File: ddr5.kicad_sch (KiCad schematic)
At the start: 39 parts, among them U1 MT60B2G8HB-48B_A

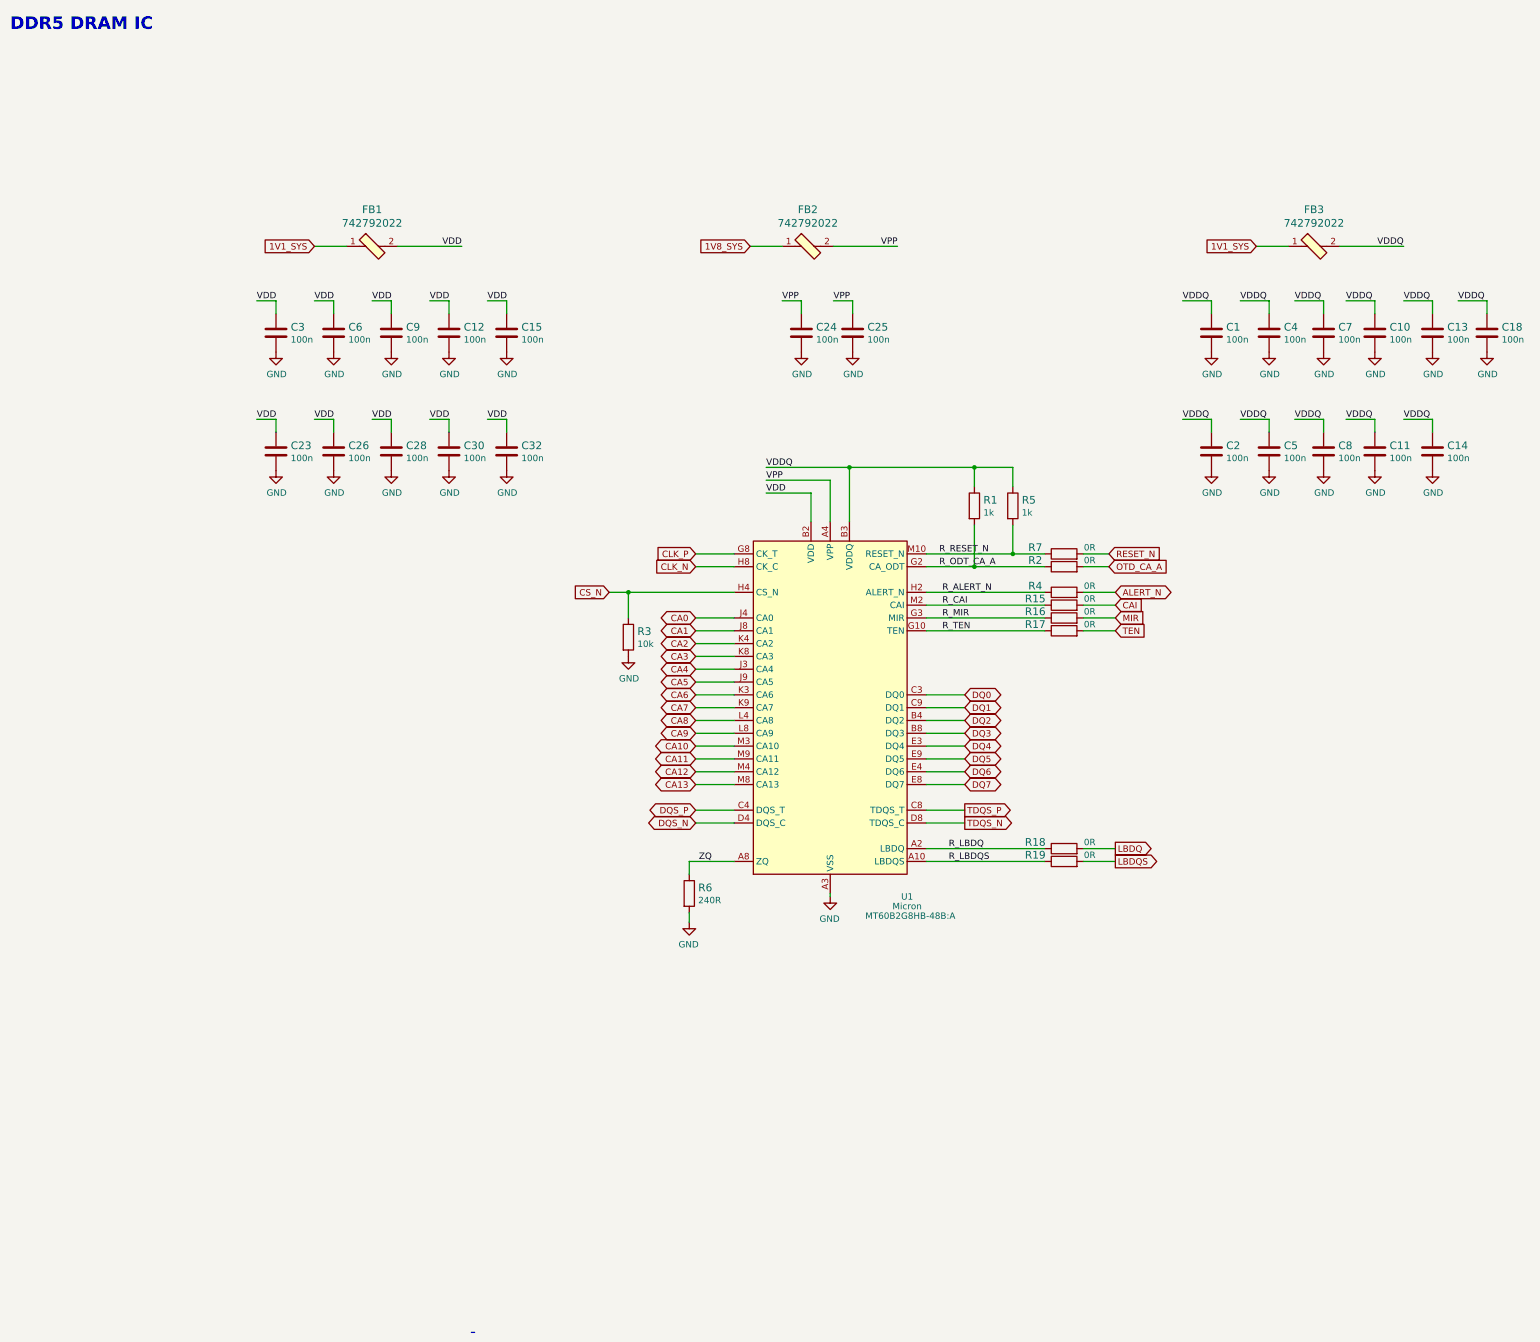
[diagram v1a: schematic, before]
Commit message: Introduce component standardization
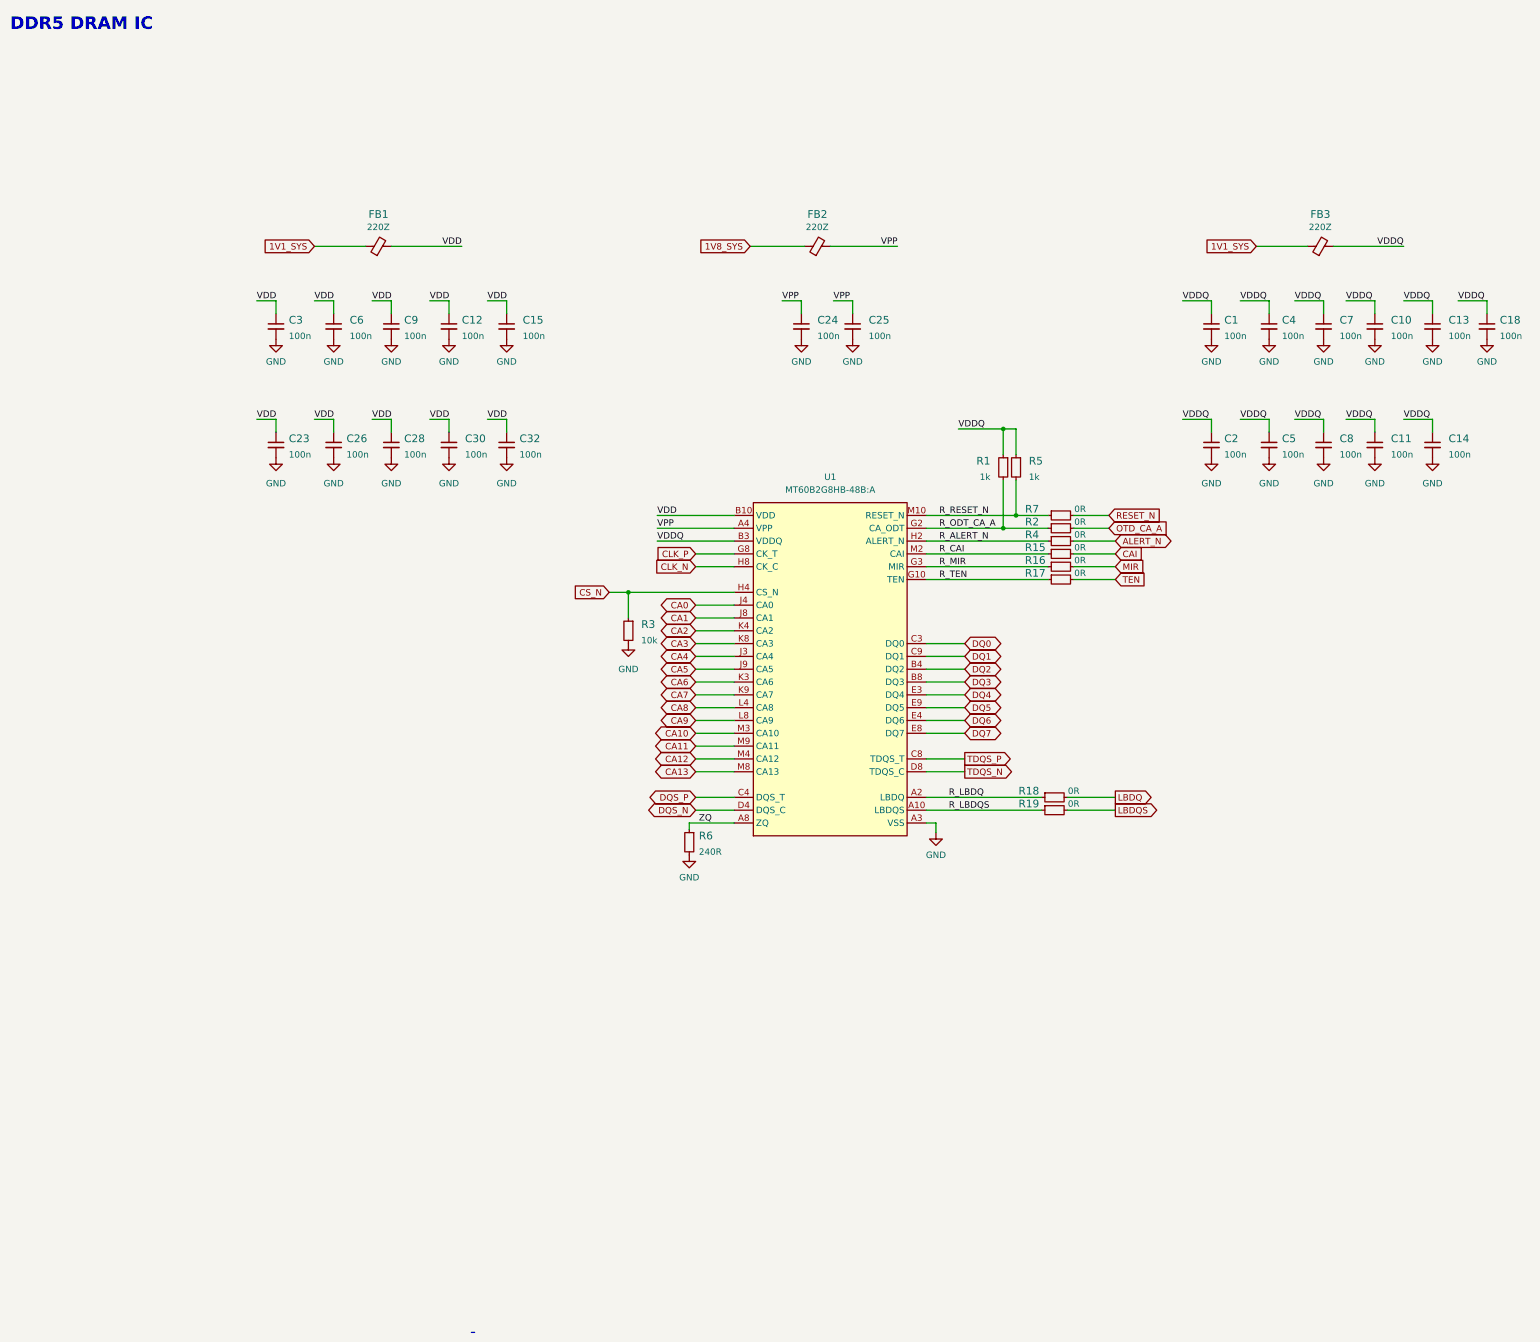
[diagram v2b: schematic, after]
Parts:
- C1, C10, C11, C12, C13, C14, C15, C18, C2, C23, C24, C25, C26, C28, C3, C30, C32, C4, C5, C6, C7, C8, C9: footprint ddr5-testbed-footprints:0201-res -> ddr5-testbed-footprints:C_0201; Author (none) -> Antmicro; License (none) -> Apache-2.0; Manufacturer YAGEO -> Yaego
- FB1, FB2, FB3: value 742792022 -> FB_220Z_1.5A_0805; footprint ddr5-testbed-footprints:0805-res -> ddr5-testbed-footprints:FB_0805_2012Metric; symbol ddr5-testbed:742792022 -> ddr5-testbed:FB_220Z_1.5A_0805; Author (none) -> Antmicro; Current (none) -> 1.5A; License (none) -> Apache-2.0; Val (none) -> 220Z
- R1, R5: footprint ddr5-testbed-footprints:0402-res -> ddr5-testbed-footprints:R_0402_1005Metric; Author (none) -> Antmicro; License (none) -> Apache-2.0; Manufacturer BOURNS -> Bourns; Tolerance (none) -> 1%
- R15, R16, R17, R18, R19, R2, R4, R7: footprint ddr5-testbed-footprints:0402-res -> ddr5-testbed-footprints:R_0402_1005Metric; Author (none) -> Antmicro; Current (none) -> 1A; License (none) -> Apache-2.0; Manufacturer PANASONIC -> Panasonic
- R3: footprint ddr5-testbed-footprints:0402-res -> ddr5-testbed-footprints:R_0402_1005Metric; Author (none) -> Antmicro; License (none) -> Apache-2.0; MPN CRCW040210K0FKEDHP -> CR0402-FX-1002GLF; Manufacturer VISHAY -> Bourns; Tolerance (none) -> 1%
- R6: value R_240R_1%_0402 -> R_240R_0402; footprint ddr5-testbed-footprints:0402-res -> ddr5-testbed-footprints:R_0402_1005Metric; symbol ddr5-testbed:R_240R_1%_0402 -> ddr5-testbed:R_240R_0402; Author (none) -> Antmicro; License (none) -> Apache-2.0; MPN RC0402FR-13240RL -> CR0402-FX-2400GLF; Manufacturer Yageo -> Bourns; Tolerance (none) -> 1%
- U1: footprint ddr5-testbed-footprints:FVBGA-82_11x13_9.0x11.0mm -> ddr5-testbed-footprints:BGA-82_11x9mm_Layout13x11_P0.8mm_DDR5_MO-210-AN; Author (none) -> Antmicro; License (none) -> Apache-2.0
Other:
- moved on the sheet: C1, C10, C11, C12, C13, C14, C15, C18, C2, C23, C24, C25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
